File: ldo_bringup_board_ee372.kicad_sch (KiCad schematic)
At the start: 53 parts, among them J1 VIN, J2 GND, J3 IBIAS, J4 VOUT, J5 VIN_SMA, J6 VOUT_SMA, J7 GND, Q1 FDV305N, Q2 FDV305N, Q3 FDV305N, Q4 FDV305N, Q5 FDV305N, SW1 SW_SPDT, U1 LDO_DualMode_BGR_EE372

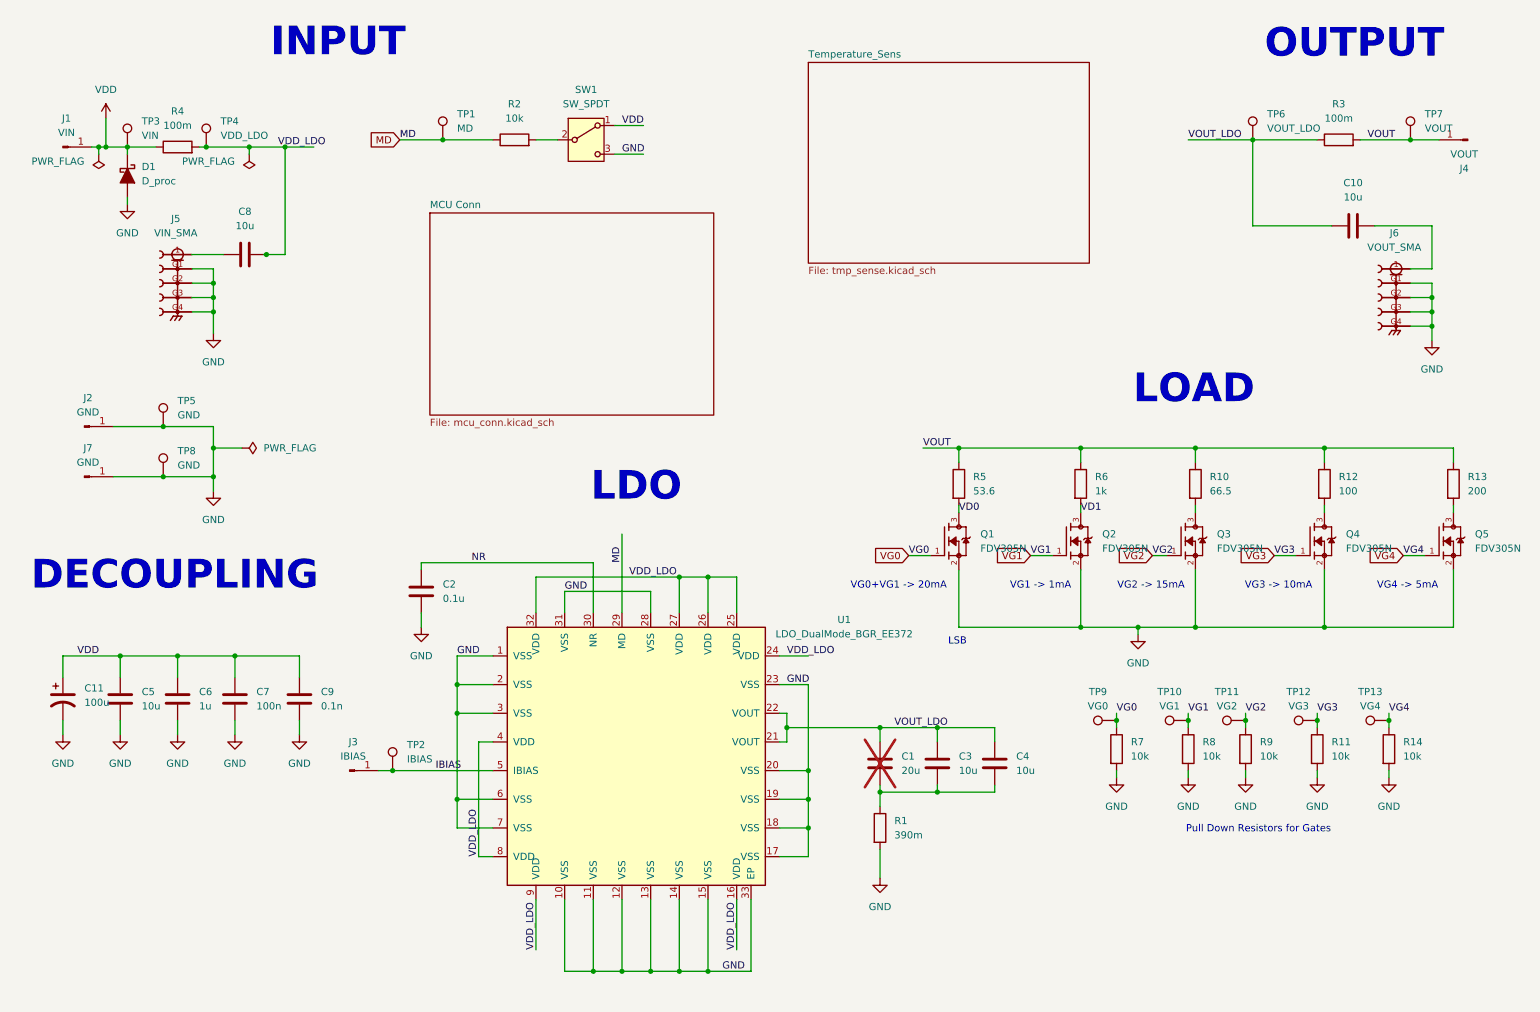
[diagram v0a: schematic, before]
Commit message: Add Teensy 4.1, current sensing, a 5 V input and MD jumpers
The netlist goes from 66 parts and 28 nets to 105 parts and 79 nets.

Schematic edits by Luke
- U2, a Teensy 4.1 on socket strips, replaces the MCU headers. Pins 2 to 6
  go to VG0 to VG4 through 0 ohm links R22 to R26. Pin 7 goes to the Q6 gate
  through jumper J9. Pins 10 to 13 carry the SPI labels. A1 and A2 read the
  two current-sense outputs.
- U3 and U4, INA190A5 amplifiers across shunts R4 and R3, through 0 ohm
  links R29 to R32. Each output has a 1k and 100n filter (R27 with C12,
  R28 with C15).
- J8 is now a +5V banana jack to the Teensy VIN, with C16 to C19 and
  Schottky D2 from +5V to GND.
- A +3V3 rail from the Teensy 3V3 pin, with C5, C13, C14, C20, C21 and C22.
- MD control uses three 2-pin jumpers, J9, J10 and J11. R15 and R16 are
  removed. R18 is the 10k pull-up behind J11.
- R19 and R20, 0 ohm across the two shunts, both marked DNP. R21, 0 ohm
  between VOUT and the load resistors.
- C6 changed from 1u 0805 to 10u 1206.
- Test points TP20 to TP29.
- Global labels SHUNT_IN_A, SHUNT_IN_B, SHUNT_OUT_A and SHUNT_OUT_B on the
  shunt nodes.

Field edits by Claude
- Footprint and part fields on the twelve 0 ohm resistors (R19 to R26, R29
  to R32), Vishay CRCW08050000Z0EAHP.
- Part fields on TP14 to TP19 and TP22 to TP29, Keystone 5005.
- Description on J9, J10 and J11.
A netlist export before and after those edits has identical nets and values.

ERC reports 0 errors and 40 warnings.

Co-Authored-By: Claude Opus 5.5 (1M context) <noreply@anthropic.com>
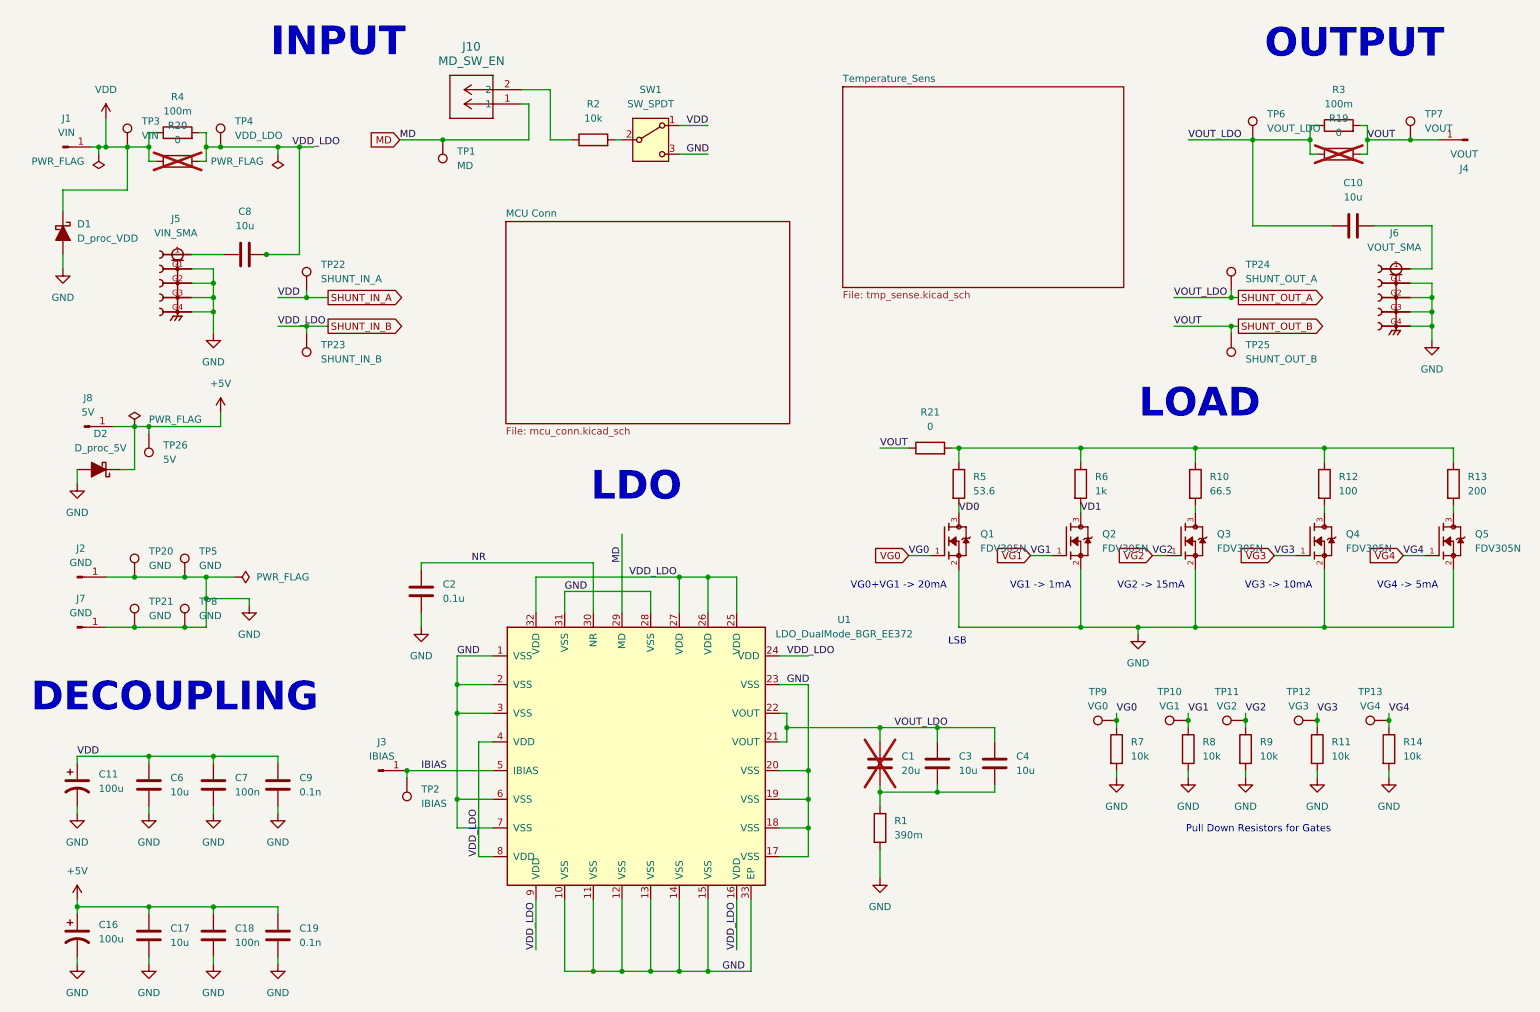
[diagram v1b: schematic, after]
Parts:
- removed C5: 10u, Capacitor_SMD:C_1206_3216Metric_Pad1.33x1.80mm_HandSolder, symbol Device:C
- added C16: 100u, Capacitor_THT:CP_Radial_D6.3mm_P2.50mm, symbol Device:C_Polarized_US
- added C17: 10u, Capacitor_SMD:C_1206_3216Metric_Pad1.33x1.80mm_HandSolder, symbol Device:C
- added C18: 100n, Capacitor_SMD:C_0805_2012Metric_Pad1.18x1.45mm_HandSolder, symbol Device:C
- added C19: 0.1n, Capacitor_SMD:C_0805_2012Metric_Pad1.18x1.45mm_HandSolder, symbol Device:C
- added D2: D_proc_5V, Diode_SMD:D_SMA_Handsoldering, symbol Device:D_Schottky_Filled
- added J10: MD_SW_EN, ldo_bringup_board_ee372:CONN_PxC02S_SUL, symbol ldo_bringup_board_ee372:PEC02SAAN
- added J8: 5V, ldo_bringup_board_ee372:CalTest_CT3151SP, symbol Connector:Conn_01x01_Pin
- added R19, R20, R21: 0, Resistor_SMD:R_0805_2012Metric_Pad1.20x1.40mm_HandSolder, symbol Device:R
- added TP20, TP21: GND, TestPoint:TestPoint_Keystone_5005-5009_Compact, symbol Connector:TestPoint
- added TP22: SHUNT_IN_A, TestPoint:TestPoint_Keystone_5005-5009_Compact, symbol Connector:TestPoint
- added TP23: SHUNT_IN_B, TestPoint:TestPoint_Keystone_5005-5009_Compact, symbol Connector:TestPoint
- added TP24: SHUNT_OUT_A, TestPoint:TestPoint_Keystone_5005-5009_Compact, symbol Connector:TestPoint
- added TP25: SHUNT_OUT_B, TestPoint:TestPoint_Keystone_5005-5009_Compact, symbol Connector:TestPoint
- added TP26: 5V, TestPoint:TestPoint_Keystone_5005-5009_Compact, symbol Connector:TestPoint
- C6: value 1u -> 10u; footprint Capacitor_SMD:C_0805_2012Metric_Pad1.18x1.45mm_HandSolder -> Capacitor_SMD:C_1206_3216Metric_Pad1.33x1.80mm_HandSolder; Distributer Link 1 https://www.digikey.com/en/products/detail/samsung-electro-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 -> https://www.digikey.com/en/products/detail/kemet/C1206C106J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; Manufacturer Samsung Electro-Mechanics -> KEMET; Manufacturer Part Number CL21B105KBFNNNE -> C1206C106J3RACAUTO
- D1: value D_proc -> D_proc_VDD
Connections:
- net GND: now also C16.2, C17.2, C18.2, C19.2, D2.2 (A), TP20.1, TP21.1
- net MD: now also J10.1; no longer R2.1
- net VDD: now also R20.1, TP22.1
- net VDD_LDO renamed SHUNT_IN_B
- net SHUNT_IN_B: now also R20.2, TP23.1
- net VOUT: no longer names the net of R10.1, R12.1, R13.1, R5.1, R6.1
- net VOUT: now also R21.2; no longer J4.1 (Pin_1), R3.2, TP7.1
- net VOUT_LDO renamed SHUNT_OUT_A
- net SHUNT_OUT_A: now also R19.1, TP24.1
- new net: J10.2, R2.1
- new net +5V: C16.1, C17.1, C18.1, C19.1, D2.1 (K), J8.1 (Pin_1), TP26.1
- new net SHUNT_OUT_B: J4.1 (Pin_1), R19.2, R21.1, R3.2, TP25.1, TP7.1
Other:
- moved on the sheet: C11, C7, C9, D1, J2, J3, J7, R2, R3, R4, SW1, TP1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
